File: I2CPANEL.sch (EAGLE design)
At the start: 26 parts, among them IC1 MCP23017SO, IC2 128X64 OLED, J1 M10-SOCKET, J2 OLED

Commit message: Routing with larger OLED for v2.0 release
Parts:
- removed IC2: 128X64 OLED, freetronics-jon:OLED-I2C128X32
- added J3: I2C, SuperHouse-Connectors:M06-PIN
- J2: value OLED -> I2C; device SuperHouse-Connectors:M04-PIN -> SuperHouse-Connectors:M06-PIN
- SJ1, SJ2, SJ3: value (none) -> SJC; device freetronics-jon:SJN -> SuperHouse-Jumpers:SJC-NORMAL
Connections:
- new net !INT: IC1.INTA, J2.6, J3.6
- new net VIN: J2.5, J3.5
- net GND: now also J3.4, MOD1.GND; no longer IC2.GND
- net SCL: now also J3.2, MOD1.SCL; no longer IC2.SCL
- net SDA: now also J3.1, MOD1.SDA; no longer IC2.SDA
- net VCC: now also J3.3, MOD1.VCC; no longer IC2.VCC
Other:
- note added: "128x64 1.3" OLED Header"
- note added: "I2C Headers"
- note removed: "128x64 OLED Header"
- note removed: "I2C Header"
- moved on the sheet: MOD1

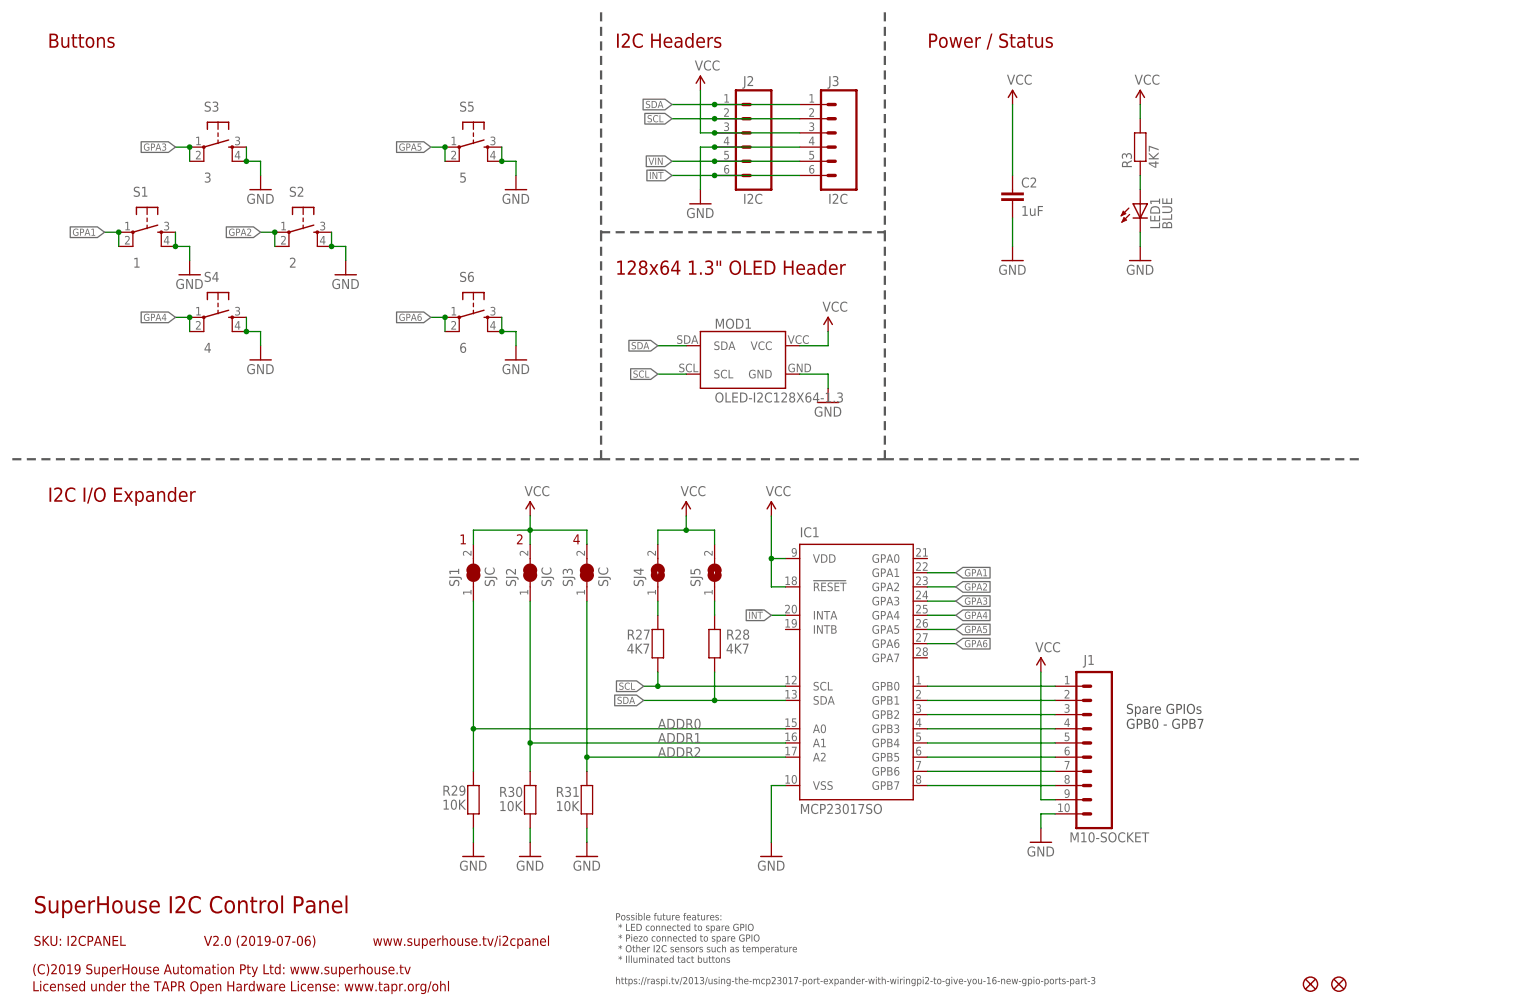
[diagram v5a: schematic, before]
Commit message: Changed to I2C-BREAKOUT header for v3.0 release
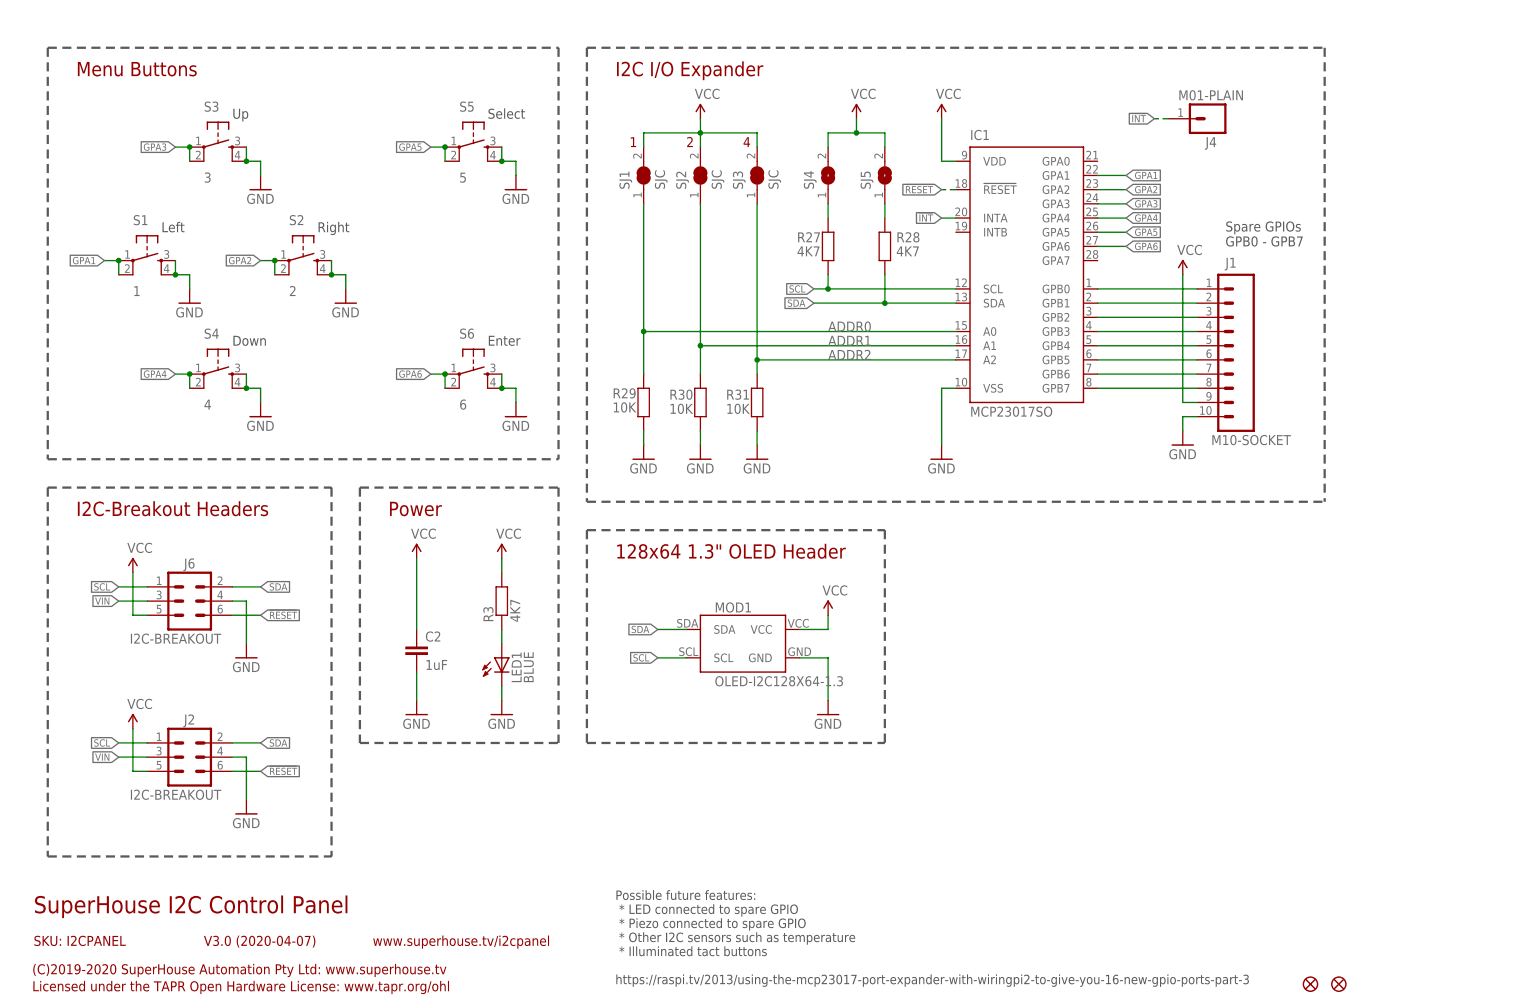
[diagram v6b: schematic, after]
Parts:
- removed J3: I2C, SuperHouse-Connectors:M06-PIN
- added J4: M01-PLAIN, SuperHouse-Connectors:M01-PLAIN
- added J6: I2C-BREAKOUT, SuperHouse-Connectors:M02X3-SHROUDED
- J2: value I2C -> I2C-BREAKOUT; device SuperHouse-Connectors:M06-PIN -> SuperHouse-Connectors:M02X3-SHROUDED
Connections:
- new net !RESET: IC1.!RESET, J2.6, J6.6
- net !INT: now also J4.1; no longer J2.6, J3.6
- net GND: now also J6.4; no longer J3.4
- net SCL: now also J2.1, J6.1; no longer J2.2, J3.2
- net SDA: now also J2.2, J6.2; no longer J2.1, J3.1
- net VCC: now also J2.5, J6.5; no longer IC1.!RESET, J2.3, J3.3
- net VIN: now also J2.3, J6.3; no longer J2.5, J3.5
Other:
- note added: "(C)2019-2020 SuperHouse Automation Pty Ltd: www.superhouse.tv"
- note added: "Down"
- note added: "Enter"
- note added: "I2C-Breakout Headers"
- note added: "Left"
- note added: "Menu Buttons"
- note added: "Power"
- note added: "Right"
- note added: "Select"
- note added: "Up"
- note added: "V3.0 (2020-04-07)"
- note removed: "(C)2019 SuperHouse Automation Pty Ltd: www.superhouse.tv"
- note removed: "Buttons"
- note removed: "I2C Headers"
- note removed: "Power / Status"
- note removed: "V2.0 (2019-07-06)"
- moved on the sheet: C2, IC1, J1, J2, LED1, MOD1, R27, R28, R29, R3, R30, R31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
